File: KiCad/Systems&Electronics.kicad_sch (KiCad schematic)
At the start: 49 parts, among them J1 Pressure Transducer, J12 Screw_Terminal_01x02, J13 Screw_Terminal_01x03, J2 Pressure Transducer, J3 Pressure Transducer, J4 Pressure Transducer, J5 Pressure Transducer, J6 Pressure Transducer

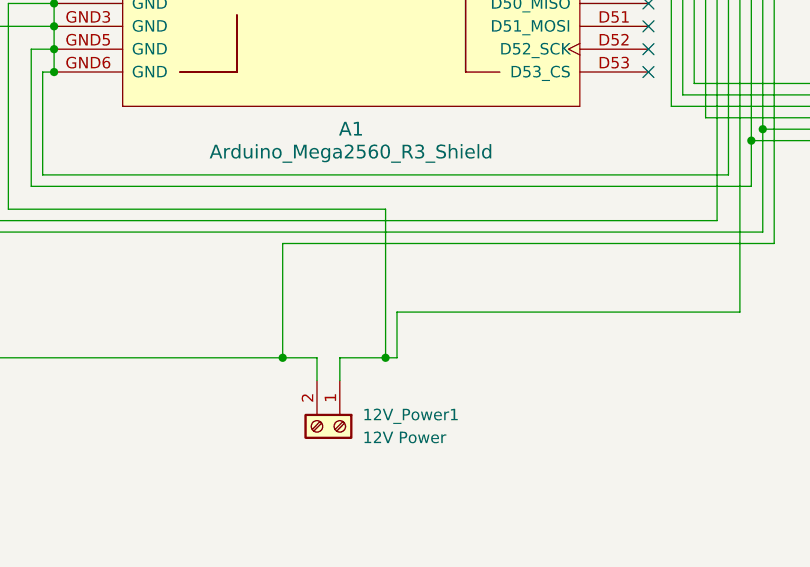
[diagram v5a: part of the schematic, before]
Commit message: PCB layout minor updates
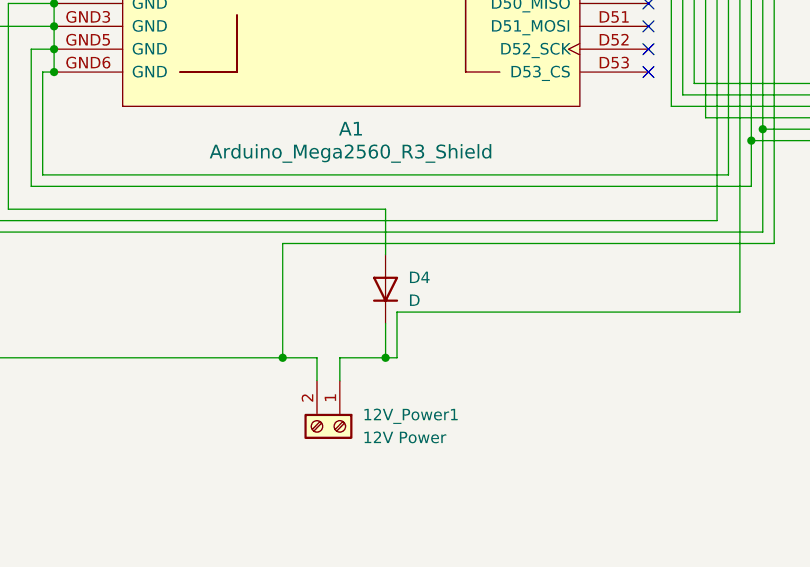
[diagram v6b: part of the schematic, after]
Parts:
- added D4: D, Diode_THT:D_A-405_P7.62mm_Horizontal, symbol Device:D
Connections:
- net at A1.GND1 (GND), A1.GND2 (GND), A1.GND3 (GND)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: now also D4.2 (A); no longer 12V_Power1.1 (Pin_1), J_Fuel1.1 (Pin_1), J_Ign1.1 (Pin_1), J_N1.1 (Pin_1), J_Oxy1.1 (Pin_1), J_Pres1.1 (Pin_1), J_Shut1.1 (Pin_1), Relay_F1.NC, Relay_Fuel_Pres1.NC, Relay_Ign1.NC, Relay_N1.NC, Relay_Oxy1.NC, Relay_Shutdown1.NC
- new net: 12V_Power1.1 (Pin_1), D4.1 (K), J_Fuel1.1 (Pin_1), J_Ign1.1 (Pin_1), J_N1.1 (Pin_1), J_Oxy1.1 (Pin_1), J_Pres1.1 (Pin_1), J_Shut1.1 (Pin_1), Relay_F1.NC, Relay_Fuel_Pres1.NC, Relay_Ign1.NC, Relay_N1.NC, Relay_Oxy1.NC, Relay_Shutdown1.NC
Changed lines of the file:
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@@
 	(wire
 		(pts
-			(xy 130.81 168.91) (xy 130.81 185.42)
+			(xy 130.81 168.91) (xy 130.81 173.99)
 		)
 		(stroke
@@
 	(wire
 		(pts
+			(xy 130.81 181.61) (xy 130.81 185.42)
+		)
+		(stroke
+			(width 0)
+			(type default)
+		)
+	)
+	(wire
+		(pts
 			(xy 218.44 93.98) (xy 222.25 93.98)
 		)
@@
 	)
 	(symbol
-		(lib_name "Sensors:AD8495_PCB")
 		(lib_id "Sensors:AD8495_PCB")
 		(at 57.15 168.91 180)
@@
 	)
 	(symbol
-		(lib_name "Sensors:AD8495_PCB")
 		(lib_id "Sensors:AD8495_PCB")
 		(at 74.93 168.91 180)
@@
 	)
 	(symbol
-		(lib_name "Sensors:AD8495_PCB")
 		(lib_id "Sensors:AD8495_PCB")
 		(at 38.1 168.91 180)
@@
 	)
 	(symbol
-		(lib_name "Sensors:AD8495_PCB")
 		(lib_id "Sensors:AD8495_PCB")
 		(at 20.32 168.91 180)
@@
 					(unit 1)
 				)
+			)
+		)
+	)
+	(symbol
+		(lib_id "Device:D")
+		(at 130.81 177.8 90)
+		(unit 1)
+		(exclude_from_sim no)
+		(in_bom yes)
+		(on_board yes)
+		(dnp no)
+		(fields_autoplaced yes)
+		(property "Reference" "D4"
+			(at 133.35 176.5299 90)
+			(effects
+				(font
+					(size 1.27 1.27)
+				)
+				(justify right)
+			)
+		)
+		(property "Value" "D"
+			(at 133.35 179.0699 90)
+			(effects
+				(font
+					(size 1.27 1.27)
+				)
+				(justify right)
+			)
+		)
+		(property "Footprint" "Diode_THT:D_A-405_P7.62mm_Horizontal"
+			(at 130.81 177.8 0)
+			(effects
+				(font
+					(size 1.27 1.27)
+				)
+				(hide yes)
+			)
+		)
+		(property "Datasheet" "~"
+			(at 130.81 177.8 0)
+			(effects
+				(font
+					(size 1.27 1.27)
+				)
+				(hide yes)
+			)
+		)
+		(property "Description" "Diode"
+			(at 130.81 177.8 0)
+			(effects
+				(font
+					(size 1.27 1.27)
+				)
+				(hide yes)
+			)
+		)
+		(property "Sim.Device" "D"
+			(at 130.81 177.8 0)
+			(effects
+				(font
+					(size 1.27 1.27)
+				)
+				(hide yes)
+			)
+		)
+		(property "Sim.Pins" "1=K 2=A"
+			(at 130.81 177.8 0)
+			(effects
+				(font
+					(size 1.27 1.27)
+				)
+				(hide yes)
+			)
+		)
+		(pin "2"
+		)
+		(pin "1"
+		)
+		(instances
+			(project ""
+				(path "/4e05caf8-77e4-4a22-9a05-51fcca8e50ff"
+					(reference "D4")
+					(unit 1)
+				)

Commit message: Footprint and PCB updates
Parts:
- R_IGN2: footprint Resistor_THT:R_Axial_Power_L48.0mm_W12.5mm_P55.88mm -> Resistor_THT:R_Axial_Power_L50.0mm_W9.0mm_P55.88mm
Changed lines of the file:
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@@
 			)
 		)
-		(property "Footprint" "Resistor_THT:R_Axial_Power_L48.0mm_W12.5mm_P55.88mm"
+		(property "Footprint" "Resistor_THT:R_Axial_Power_L50.0mm_W9.0mm_P55.88mm"
 			(at 217.17 50.038 90)
 			(effects
